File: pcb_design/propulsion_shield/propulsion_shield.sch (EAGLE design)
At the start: 64 parts

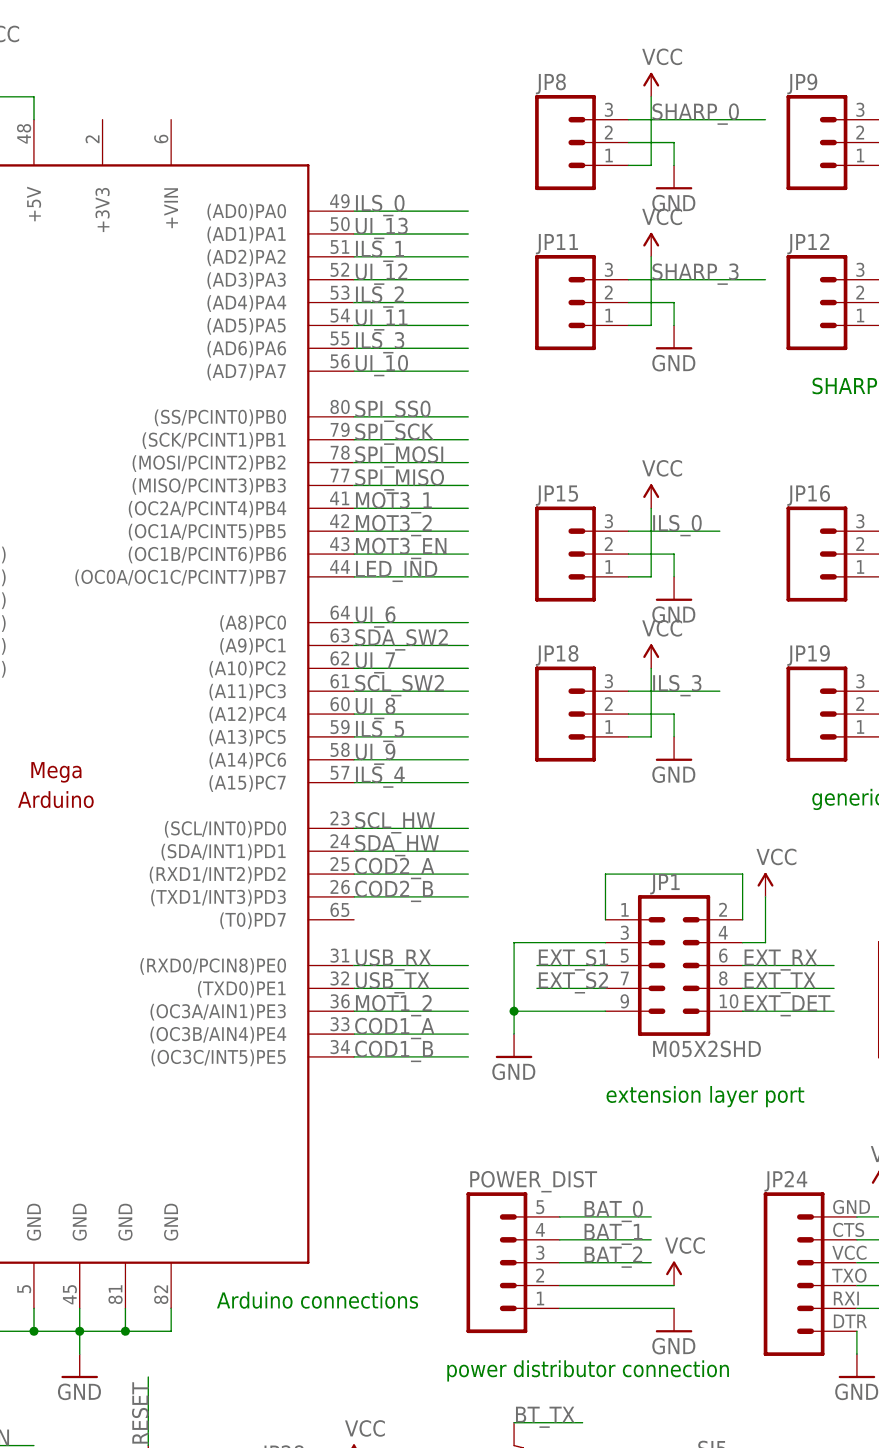
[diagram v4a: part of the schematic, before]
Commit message: [PCB/propulsion_shield] Correction routing of power supply to Vin arduino pin (schematics + PCB)
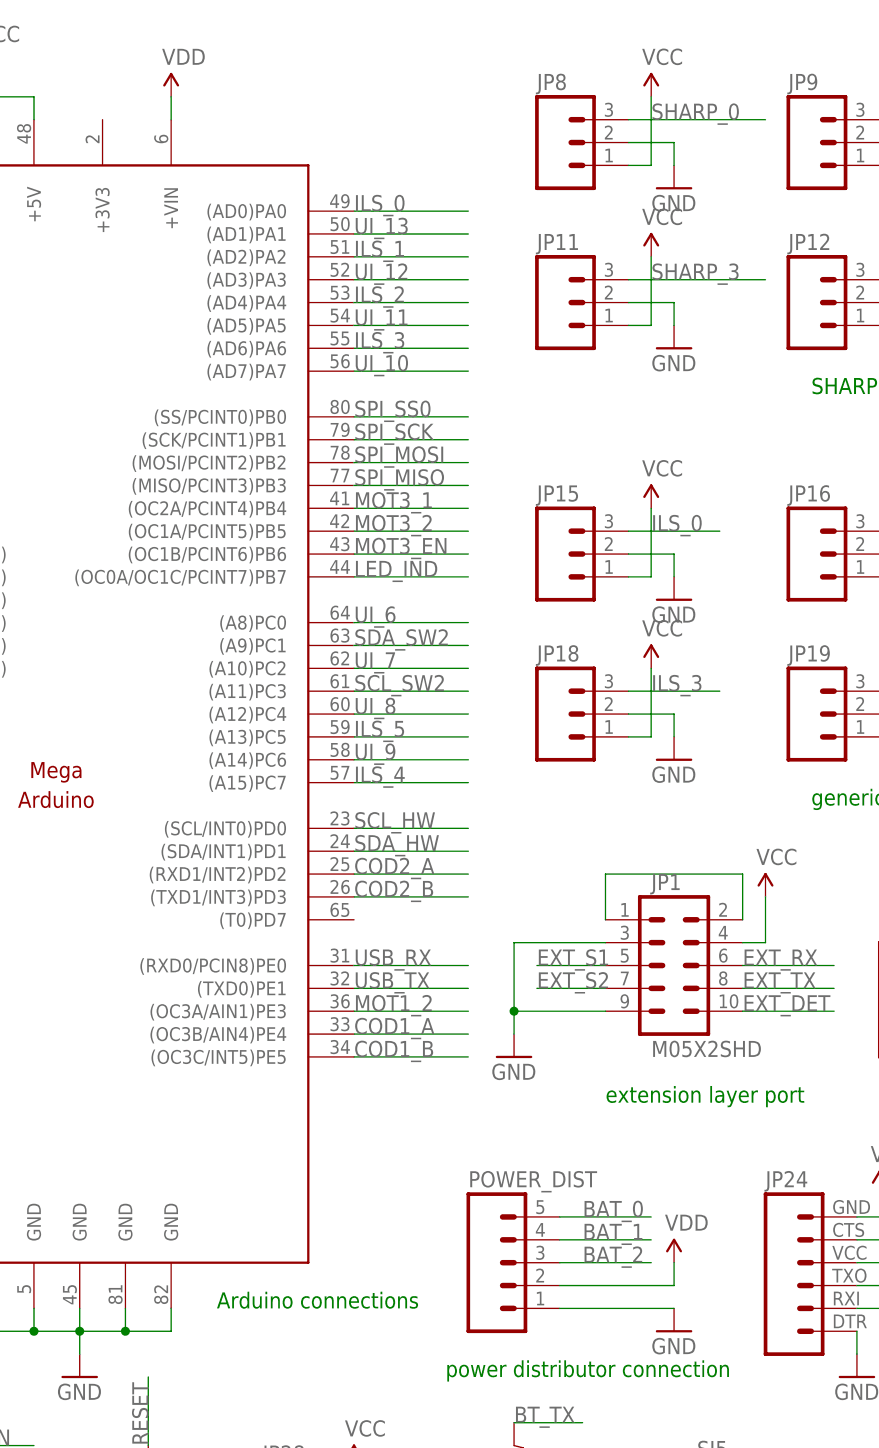
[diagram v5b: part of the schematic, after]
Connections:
- new net VDD: IC1.+VIN, POWER_DIST.2
- net VCC: no longer POWER_DIST.2
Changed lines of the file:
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@@
 <grid distance="0.1" unitdist="inch" unit="inch" style="lines" multiple="1" display="no" altdistance="0.01" altunitdist="inch" altunit="inch"/>
 <layers>
-<layer number="1" name="Top" color="4" fill="1" visible="no" active="no"/>
-<layer number="16" name="Bottom" color="1" fill="1" visible="no" active="no"/>
-<layer number="17" name="Pads" color="2" fill="1" visible="no" active="no"/>
-<layer number="18" name="Vias" color="2" fill="1" visible="no" active="no"/>
-<layer number="19" name="Unrouted" color="6" fill="1" visible="no" active="no"/>
-<layer number="20" name="Dimension" color="15" fill="1" visible="no" active="no"/>
-<layer number="21" name="tPlace" color="7" fill="1" visible="no" active="no"/>
-<layer number="22" name="bPlace" color="7" fill="1" visible="no" active="no"/>
-<layer number="23" name="tOrigins" color="15" fill="1" visible="no" active="no"/>
-<layer number="24" name="bOrigins" color="15" fill="1" visible="no" active="no"/>
-<layer number="25" name="tNames" color="7" fill="1" visible="no" active="no"/>
-<layer number="26" name="bNames" color="7" fill="1" visible="no" active="no"/>
-<layer number="27" name="tValues" color="7" fill="1" visible="no" active="no"/>
-<layer number="28" name="bValues" color="7" fill="1" visible="no" active="no"/>
+<layer number="1" name="Top" color="4" fill="1" visible="yes" active="no"/>
+<layer number="16" name="Bottom" color="1" fill="1" visible="yes" active="no"/>
+<layer number="17" name="Pads" color="2" fill="1" visible="yes" active="no"/>
+<layer number="18" name="Vias" color="2" fill="1" visible="yes" active="no"/>
+<layer number="19" name="Unrouted" color="6" fill="1" visible="yes" active="no"/>
+<layer number="20" name="Dimension" color="15" fill="1" visible="yes" active="no"/>
+<layer number="21" name="tPlace" color="16" fill="1" visible="yes" active="no"/>
+<layer number="22" name="bPlace" color="14" fill="1" visible="yes" active="no"/>
+<layer number="23" name="tOrigins" color="15" fill="1" visible="yes" active="no"/>
+<layer number="24" name="bOrigins" color="15" fill="1" visible="yes" active="no"/>
+<layer number="25" name="tNames" color="7" fill="1" visible="yes" active="no"/>
+<layer number="26" name="bNames" color="7" fill="1" visible="yes" active="no"/>
+<layer number="27" name="tValues" color="7" fill="1" visible="yes" active="no"/>
+<layer number="28" name="bValues" color="7" fill="1" visible="yes" active="no"/>
 <layer number="29" name="tStop" color="7" fill="3" visible="no" active="no"/>
 <layer number="30" name="bStop" color="7" fill="6" visible="no" active="no"/>
@@
 <layer number="35" name="tGlue" color="7" fill="4" visible="no" active="no"/>
 <layer number="36" name="bGlue" color="7" fill="5" visible="no" active="no"/>
-<layer number="37" name="tTest" color="7" fill="1" visible="no" active="no"/>
-<layer number="38" name="bTest" color="7" fill="1" visible="no" active="no"/>
+<layer number="37" name="tTest" color="7" fill="1" visible="yes" active="no"/>
+<layer number="38" name="bTest" color="7" fill="1" visible="yes" active="no"/>
 <layer number="39" name="tKeepout" color="4" fill="11" visible="no" active="no"/>
 <layer number="40" name="bKeepout" color="1" fill="11" visible="no" active="no"/>
@@
 <layer number="44" name="Drills" color="7" fill="1" visible="no" active="no"/>
 <layer number="45" name="Holes" color="7" fill="1" visible="no" active="no"/>
-<layer number="46" name="Milling" color="3" fill="1" visible="no" active="no"/>
-<layer number="47" name="Measures" color="7" fill="1" visible="no" active="no"/>
-<layer number="48" name="Document" color="7" fill="1" visible="no" active="no"/>
-<layer number="49" name="Reference" color="7" fill="1" visible="no" active="no"/>
-<layer number="50" name="dxf" color="7" fill="1" visible="no" active="no"/>
-<layer number="51" name="tDocu" color="7" fill="1" visible="no" active="no"/>
-<layer number="52" name="bDocu" color="7" fill="1" visible="no" active="no"/>
-<layer number="53" name="tGND_GNDA" color="7" fill="9" visible="no" active="no"/>
-<layer number="54" name="bGND_GNDA" color="1" fill="9" visible="no" active="no"/>
-<layer number="56" name="wert" color="7" fill="1" visible="no" active="no"/>
-<layer number="57" name="tCAD" color="7" fill="1" visible="no" active="no"/>
+<layer number="46" name="Milling" color="3" fill="1" visible="yes" active="no"/>
+<layer number="47" name="Measures" color="7" fill="1" visible="yes" active="no"/>
+<layer number="48" name="Document" color="7" fill="1" visible="yes" active="no"/>
+<layer number="49" name="Reference" color="7" fill="1" visible="yes" active="no"/>
+<layer number="50" name="dxf" color="7" fill="1" visible="yes" active="no"/>
+<layer number="51" name="tDocu" color="6" fill="1" visible="yes" active="no"/>
+<layer number="52" name="bDocu" color="7" fill="1" visible="yes" active="no"/>
+<layer number="53" name="tGND_GNDA" color="7" fill="9" visible="yes" active="no"/>
+<layer number="54" name="bGND_GNDA" color="1" fill="9" visible="yes" active="no"/>
+<layer number="56" name="wert" color="7" fill="1" visible="yes" active="no"/>
+<layer number="57" name="tCAD" color="7" fill="1" visible="yes" active="no"/>
 <layer number="90" name="Modules" color="5" fill="1" visible="yes" active="yes"/>
 <layer number="91" name="Nets" color="2" fill="1" visible="yes" active="yes"/>
@@
 <part name="POWER_DIST" library="SparkFun-Connectors" deviceset="M05" device="PTH"/>
 <part name="GND1" library="SparkFun-Aesthetics" deviceset="GND" device=""/>
-<part name="SUPPLY1" library="SparkFun-Aesthetics" deviceset="VCC" device=""/>
 <part name="JP1" library="SparkFun-Connectors" deviceset="M05X2" device="SHD"/>
 <part name="SUPPLY3" library="SparkFun-Aesthetics" deviceset="VCC" device=""/>
@@
 <part name="JP29" library="SparkFun-Connectors" deviceset="M02" device="PTH"/>
 <part name="GND36" library="SparkFun-Aesthetics" deviceset="GND" device=""/>
+<part name="SUPPLY31" library="SparkFun-Aesthetics" deviceset="VDD" device=""/>
+<part name="SUPPLY32" library="SparkFun-Aesthetics" deviceset="VDD" device=""/>
 </parts>
 <sheets>
@@
 <instance part="POWER_DIST" gate="G$1" x="96.52" y="40.64"/>
 <instance part="GND1" gate="1" x="116.84" y="33.02"/>
-<instance part="SUPPLY1" gate="G$1" x="116.84" y="38.1"/>
 <instance part="JP1" gate="G$1" x="116.84" y="73.66"/>
 <instance part="SUPPLY3" gate="G$1" x="127" y="81.28"/>
@@
 <instance part="JP29" gate="G$1" x="134.62" y="10.16"/>
 <instance part="GND36" gate="1" x="144.78" y="5.08"/>
+<instance part="SUPPLY31" gate="VDD" x="60.96" y="170.18"/>
+<instance part="SUPPLY32" gate="VDD" x="116.84" y="40.64"/>
 </instances>
 <busses>
@@
 <wire x1="45.72" y1="170.18" x2="40.64" y2="170.18" width="0.2032" layer="91"/>
 <junction x="40.64" y="170.18"/>
-</segment>
-<segment>
-<pinref part="POWER_DIST" gate="G$1" pin="2"/>
-<pinref part="SUPPLY1" gate="G$1" pin="VCC"/>
-<wire x1="104.14" y1="38.1" x2="116.84" y2="38.1" width="0.1524" layer="91"/>
 </segment>
 <segment>
@@
 </segment>
 </net>
+<net name="VDD" class="0">
+<segment>
+<pinref part="POWER_DIST" gate="G$1" pin="2"/>
+<pinref part="SUPPLY32" gate="VDD" pin="VDD"/>
+<wire x1="104.14" y1="38.1" x2="116.84" y2="38.1" width="0.1524" layer="91"/>
+<wire x1="116.84" y1="38.1" x2="116.84" y2="40.64" width="0.1524" layer="91"/>
+</segment>
+<segment>
+<pinref part="IC1" gate="G$1" pin="+VIN"/>
+<pinref part="SUPPLY31" gate="VDD" pin="VDD"/>
+<wire x1="60.96" y1="167.64" x2="60.96" y2="170.18" width="0.1524" layer="91"/>
+</segment>
+</net>
